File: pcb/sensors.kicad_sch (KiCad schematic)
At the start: 19 parts, among them IC3 ICM-45686, IC4 ICM-45686, IC5 MMC5983MA, U3 BMP581, U5 H3LIS331DLTR

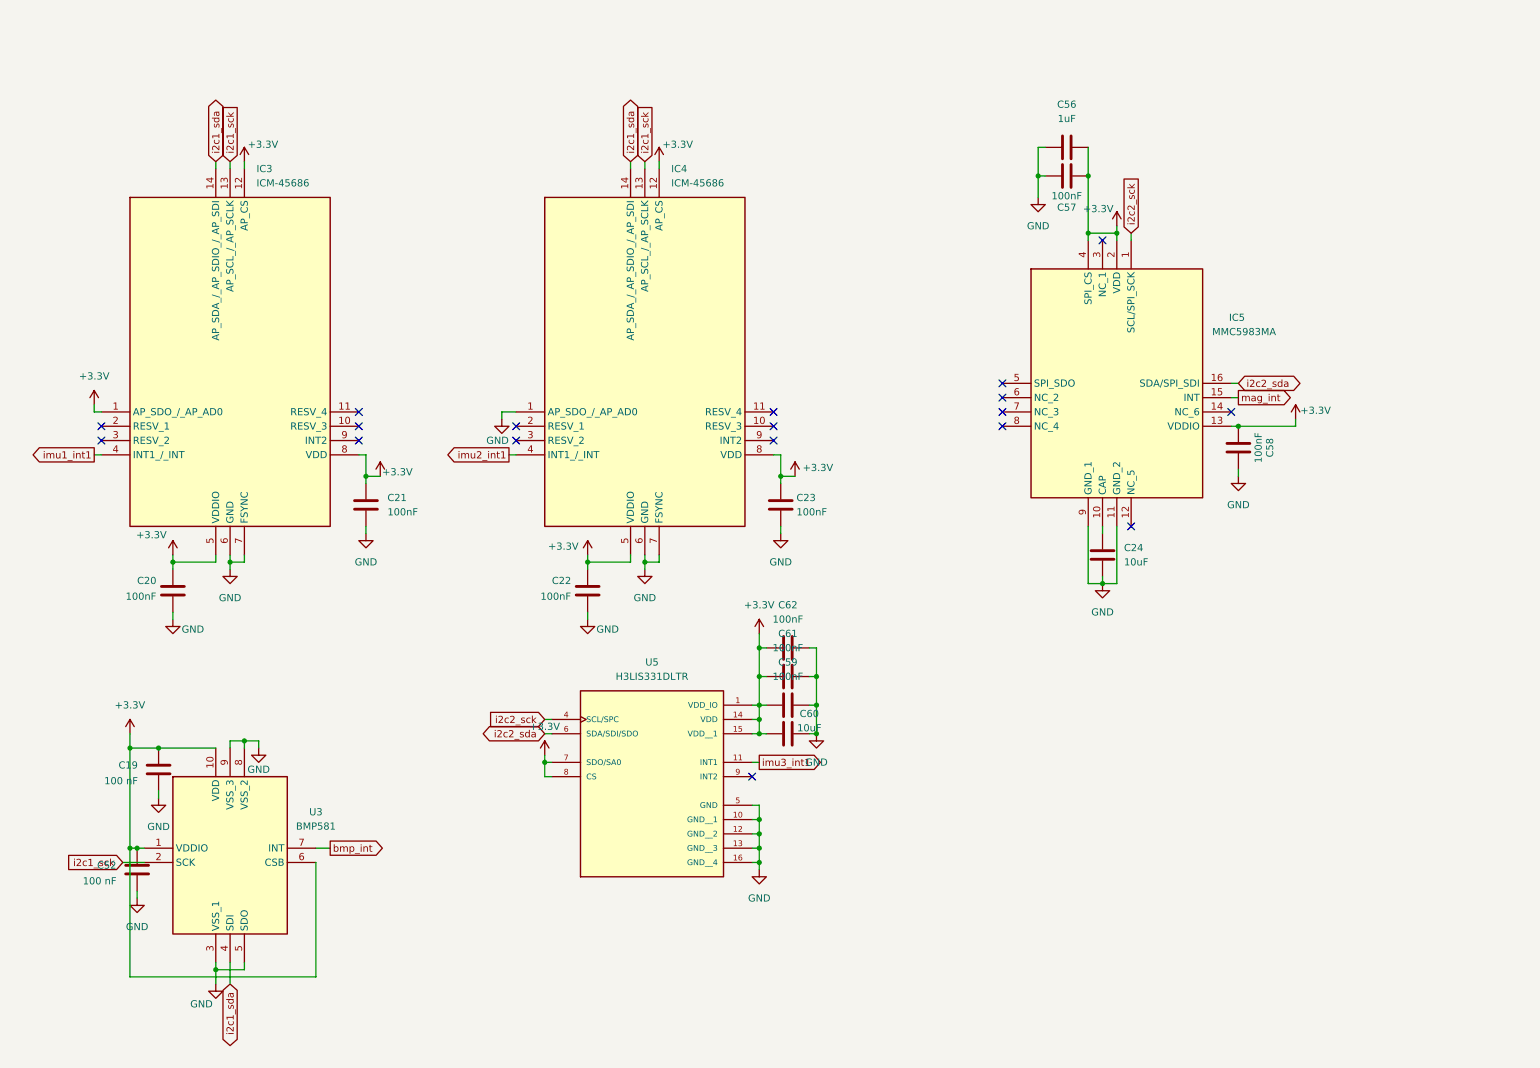
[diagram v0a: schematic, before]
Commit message: added models for some things, fixed micro sd impl and a bunch of other stuff - pcb currently probably ready for production
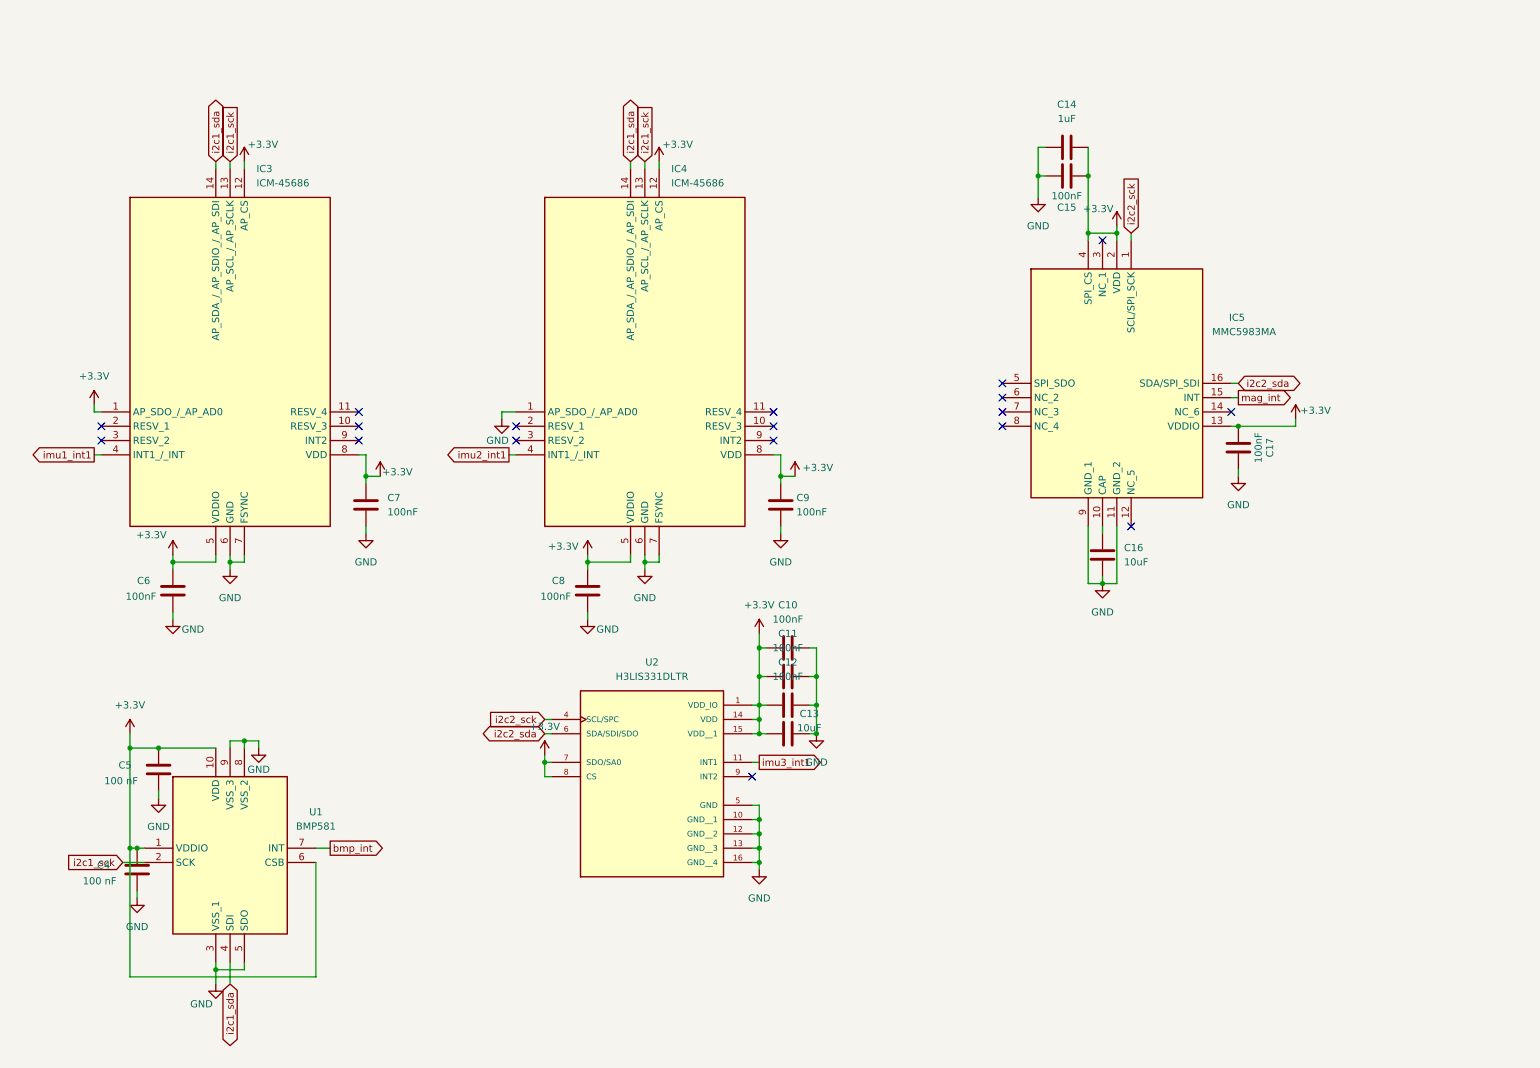
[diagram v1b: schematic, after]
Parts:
- renumbered C62 to C10, C61 to C11, C59 to C12, C60 to C13, C56 to C14, C57 to C15, C24 to C16, C58 to C17, C52 to C4, C19 to C5, C20 to C6, C21 to C7, C22 to C8, C23 to C9, U3 to U1, U5 to U2

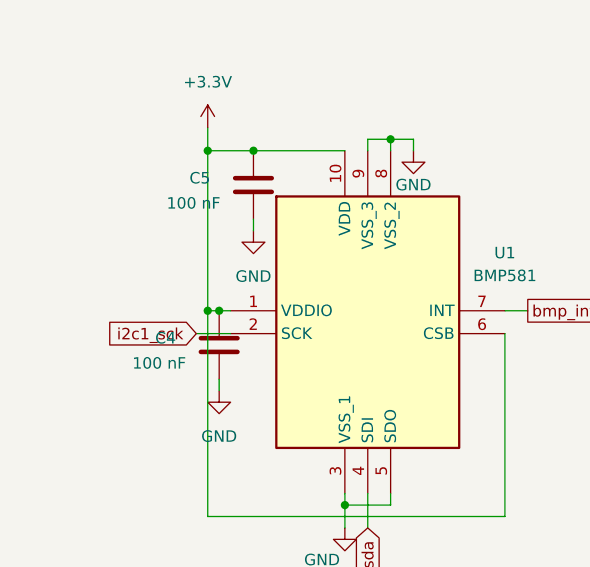
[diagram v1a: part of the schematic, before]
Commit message: started making bom - changed some stuff for compatibility with it
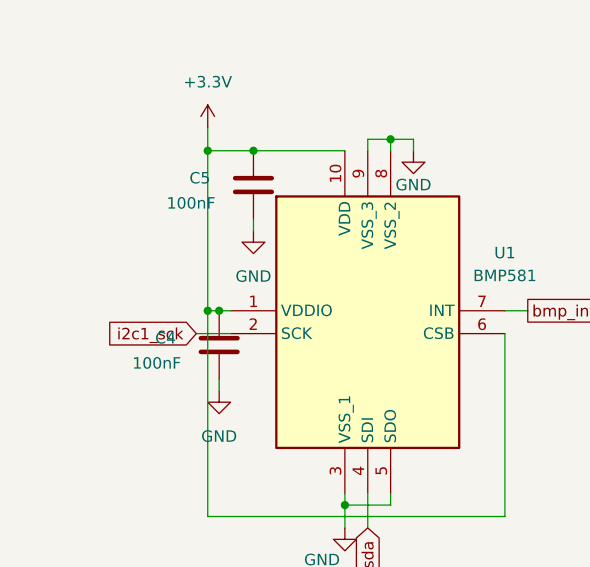
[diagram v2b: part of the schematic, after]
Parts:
- C4, C5: value 100 nF -> 100nF
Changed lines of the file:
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@@
 			)
 		)
-		(property "Value" "100 nF"
+		(property "Value" "100nF"
 			(at 25.908 167.132 0)
 			(effects
@@
 			)
 		)
-		(property "Value" "100 nF"
+		(property "Value" "100nF"
 			(at 29.718 149.352 0)
 			(effects

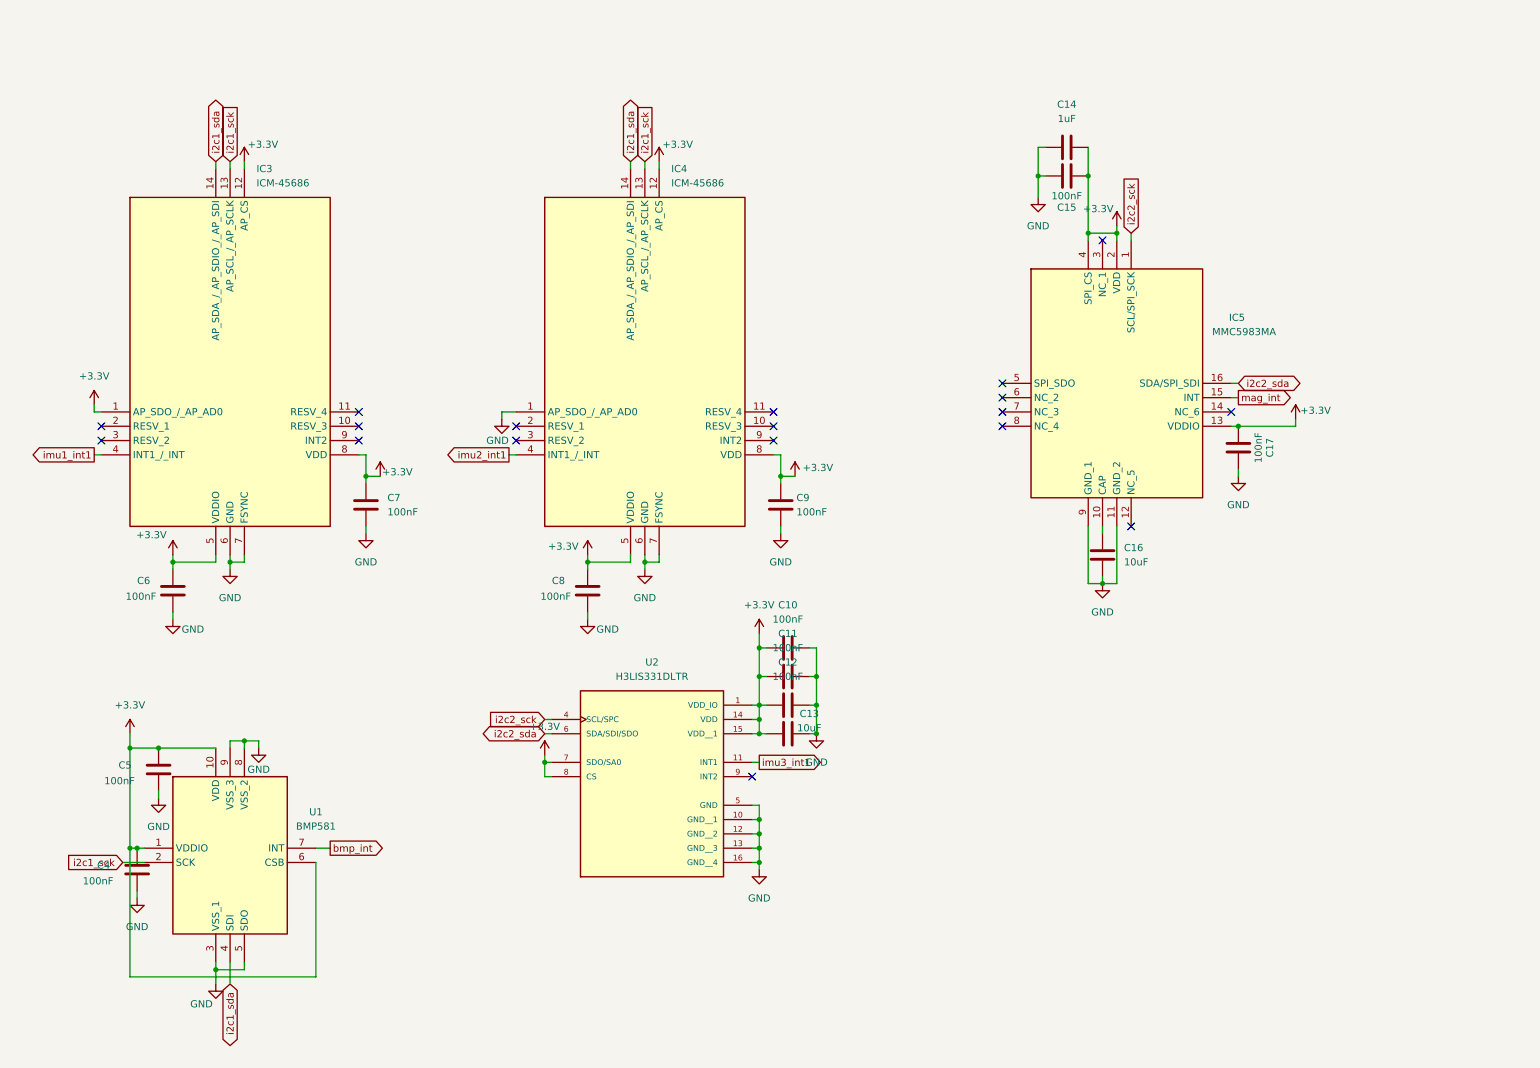
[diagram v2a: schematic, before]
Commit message: reorganized schematic, started to add a readme (not really though), also pcb updated
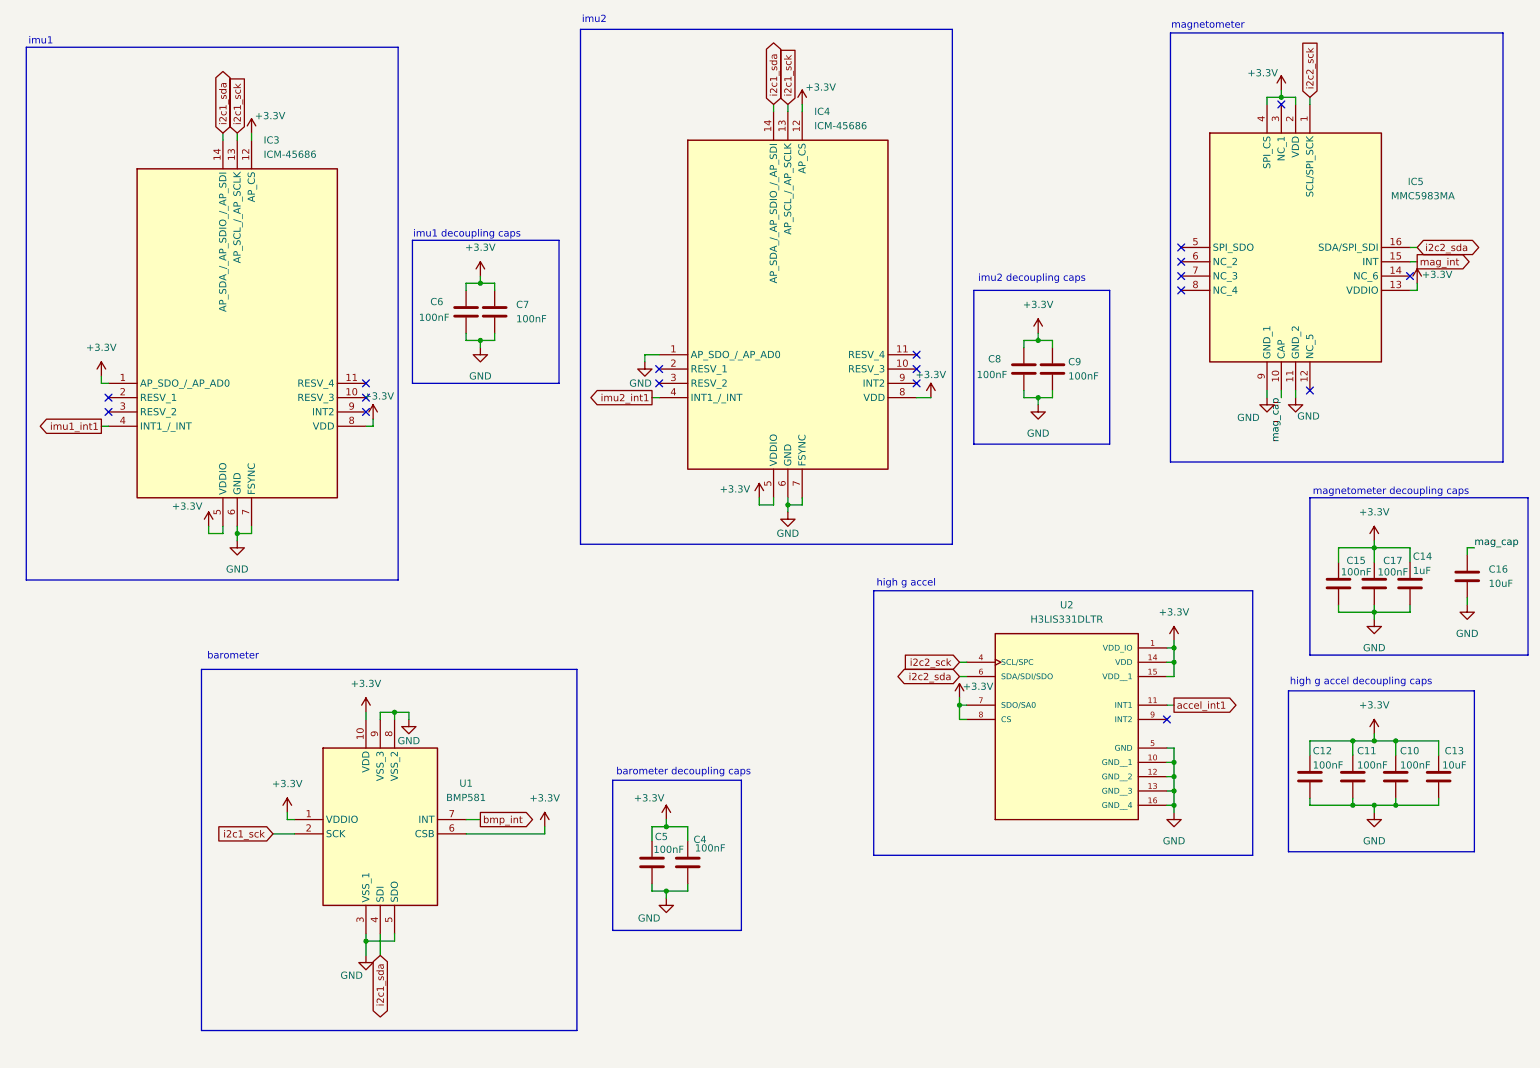
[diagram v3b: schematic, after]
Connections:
- net +3.3V: now also C10.2, C11.2, C12.2, C13.2; no longer C10.1, C11.1, C12.1, C13.1
- net GND: now also C10.1, C11.1, C12.1, C13.1; no longer C10.2, C11.2, C12.2, C13.2
- net mag_cap: now reaches C16.1, IC5.10 (CAP)
- net imu3_int1 renamed accel_int1
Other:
- note added: "barometer"
- note added: "barometer decoupling caps"
- note added: "high g accel"
- note added: "high g accel decoupling caps"
- note added: "imu1"
- note added: "imu1 decoupling caps"
- note added: "imu2"
- note added: "imu2 decoupling caps"
- note added: "magnetometer"
- note added: "magnetometer decoupling caps"
- moved on the sheet: C10, C11, C12, C13, C14, C15, C16, C17, C4, C5, C6, C7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

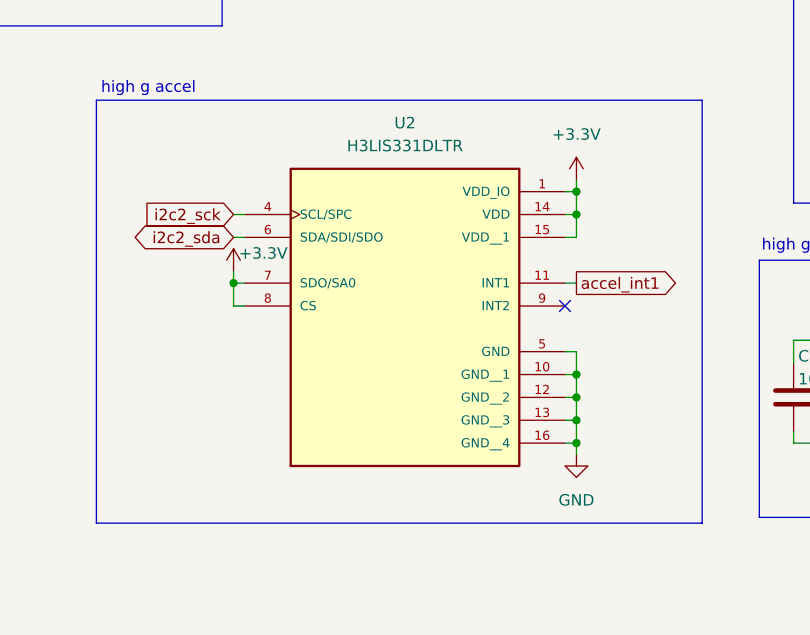
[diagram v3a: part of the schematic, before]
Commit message: fixed micro sd pullups
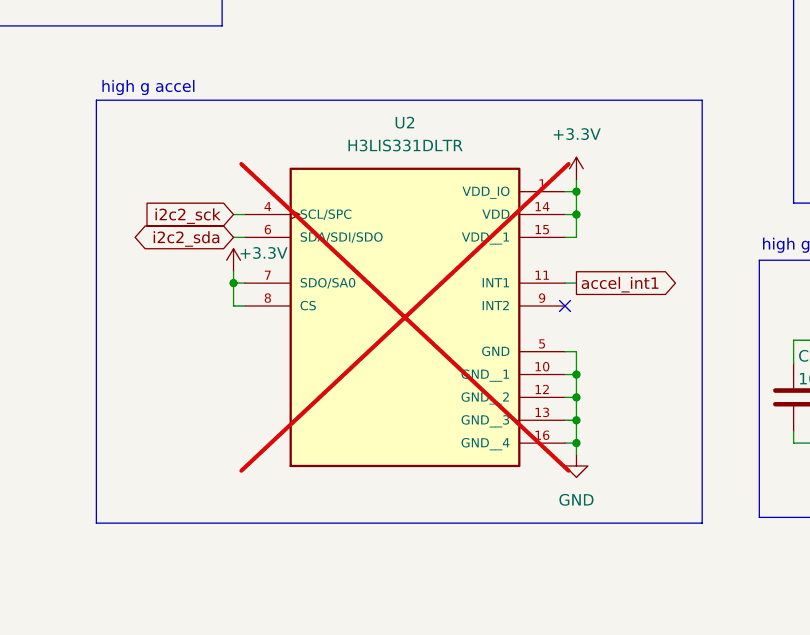
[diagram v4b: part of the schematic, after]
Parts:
- U2: now not fitted
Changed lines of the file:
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@@
 		(in_bom yes)
 		(on_board yes)
-		(dnp no)
+		(dnp yes)
 		(fields_autoplaced yes)
 		(property "Reference" "U2"
